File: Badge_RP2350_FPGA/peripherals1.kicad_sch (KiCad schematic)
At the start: 19 parts

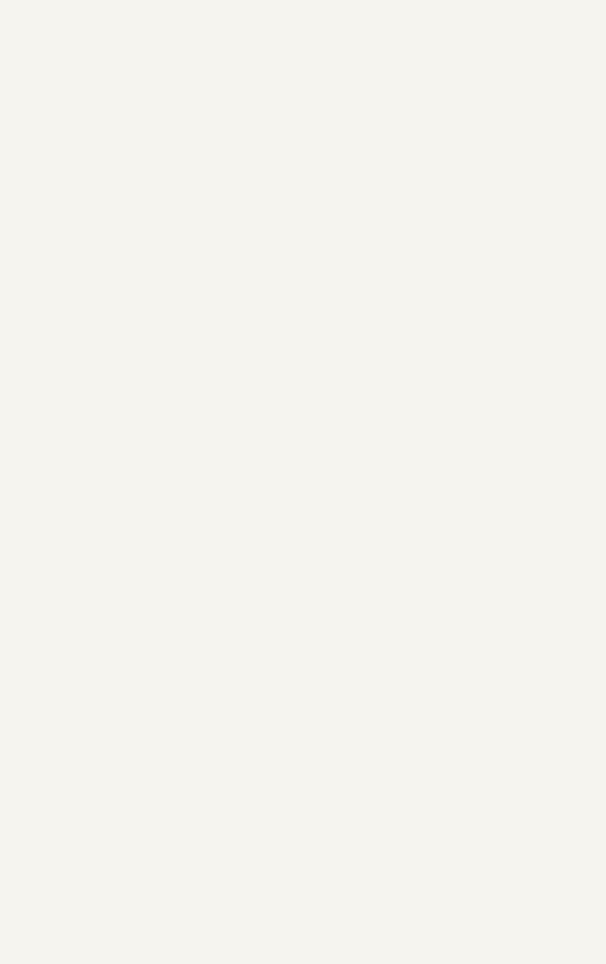
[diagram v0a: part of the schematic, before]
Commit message: add headers and fix voltage references
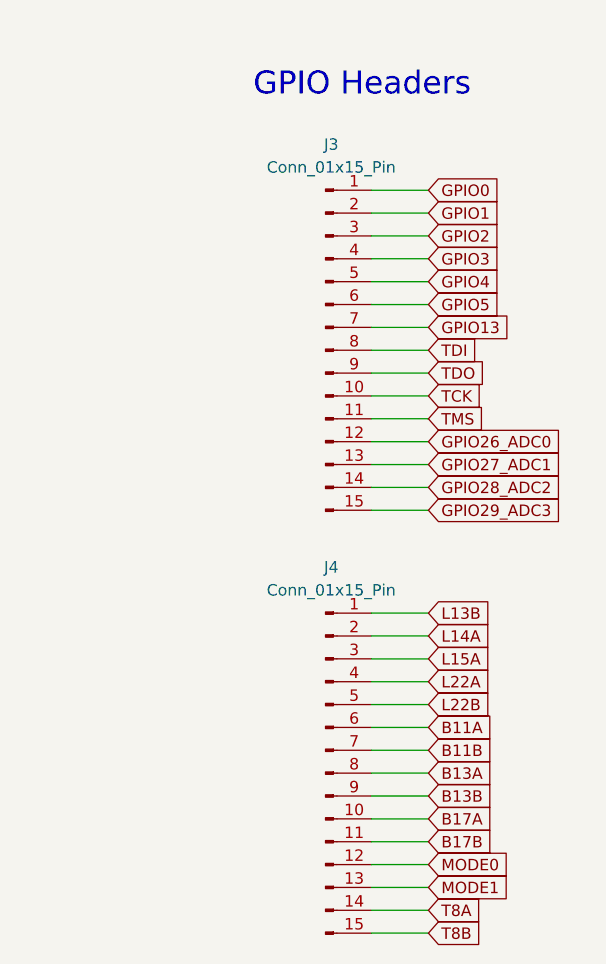
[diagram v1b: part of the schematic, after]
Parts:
- added J3, J4: Conn_01x15_Pin, Connector_PinHeader_2.54mm:PinHeader_1x15_P2.54mm_Vertical, symbol Connector:Conn_01x15_Pin
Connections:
- new net B11A: J4.6 (Pin_6)
- new net B11B: J4.7 (Pin_7)
- new net B13A: J4.8 (Pin_8)
- new net B13B: J4.9 (Pin_9)
- new net B17A: J4.10 (Pin_10)
- new net B17B: J4.11 (Pin_11)
- new net GPIO0: J3.1 (Pin_1)
- new net GPIO1: J3.2 (Pin_2)
- new net GPIO13: J3.7 (Pin_7)
- new net GPIO2: J3.3 (Pin_3)
- new net GPIO26_ADC0: J3.12 (Pin_12)
- new net GPIO27_ADC1: J3.13 (Pin_13)
- new net GPIO28_ADC2: J3.14 (Pin_14)
- new net GPIO29_ADC3: J3.15 (Pin_15)
- new net GPIO3: J3.4 (Pin_4)
- new net GPIO4: J3.5 (Pin_5)
- new net GPIO5: J3.6 (Pin_6)
- new net L13B: J4.1 (Pin_1)
- new net L14A: J4.2 (Pin_2)
- new net L15A: J4.3 (Pin_3)
- new net L22A: J4.4 (Pin_4)
- new net L22B: J4.5 (Pin_5)
- new net MODE0: J4.12 (Pin_12)
- new net MODE1: J4.13 (Pin_13)
- new net T8A: J4.14 (Pin_14)
- new net T8B: J4.15 (Pin_15)
- new net TCK: J3.10 (Pin_10)
- new net TDI: J3.8 (Pin_8)
- new net TDO: J3.9 (Pin_9)
- new net TMS: J3.11 (Pin_11)
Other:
- note added: "GPIO Headers"

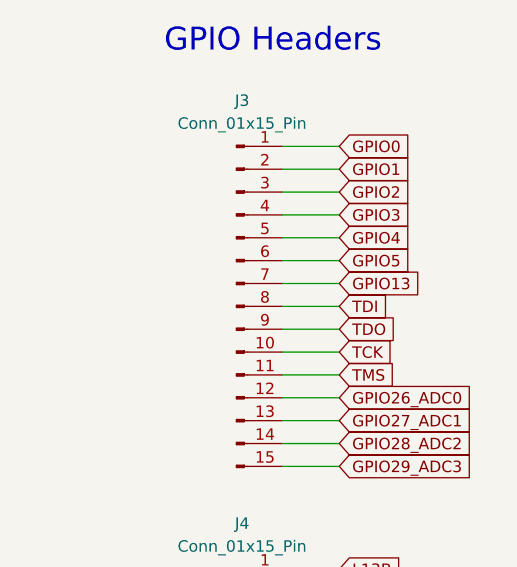
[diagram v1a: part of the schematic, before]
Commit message: add jtagsel_n connection
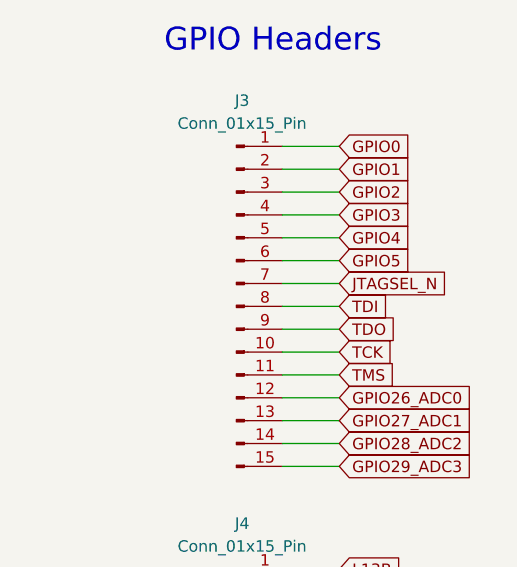
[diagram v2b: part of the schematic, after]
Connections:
- net GPIO13 renamed JTAGSEL_N
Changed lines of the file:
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@@
 		(title "RISC-V Summit Europe Badge")
 		(date "2026-03-29")
-		(rev "v1.4")
+		(rev "v1.42")
 		(company "SemiTO-V, RISC-V Student Team")
 		(comment 3 "License: CERN-OHL-W-2.0")
@@
 		)
 	)
-	(global_label "GPIO13"
+	(global_label "T8A"
+		(shape input)
+		(at 177.8 119.38 0)
+		(fields_autoplaced yes)
+		(effects
+			(font
+				(size 1.27 1.27)
+			)
+			(justify left)
+		)
+		(property "Intersheetrefs" "${INTERSHEET_REFS}"
+			(at 184.0509 119.38 0)
+			(hide yes)
+			(show_name no)
+			(do_not_autoplace no)
+			(effects
+				(font
+					(size 1.27 1.27)
+				)
+				(justify left)
+			)
+		)
+	)
+	(global_label "JTAGSEL_N"
 		(shape input)
 		(at 177.8 54.61 0)
@@
 		)
 		(property "Intersheetrefs" "${INTERSHEET_REFS}"
-			(at 187.6795 54.61 0)
-			(hide yes)
-			(show_name no)
-			(do_not_autoplace no)
-			(effects
-				(font
-					(size 1.27 1.27)
-				)
-				(justify left)
-			)
-		)
-	)
-	(global_label "T8A"
-		(shape input)
-		(at 177.8 119.38 0)
-		(fields_autoplaced yes)
-		(effects
-			(font
-				(size 1.27 1.27)
-			)
-			(justify left)
-		)
-		(property "Intersheetrefs" "${INTERSHEET_REFS}"
-			(at 184.0509 119.38 0)
-			(hide yes)
-			(show_name no)
+			(at 190.7637 54.61 0)
+			(hide yes)
+			(show_name no)

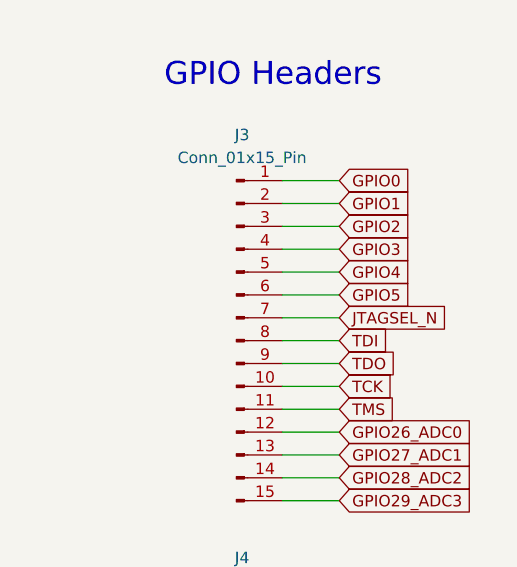
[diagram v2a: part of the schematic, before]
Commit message: add more FPGA connections and generate netlist, bom
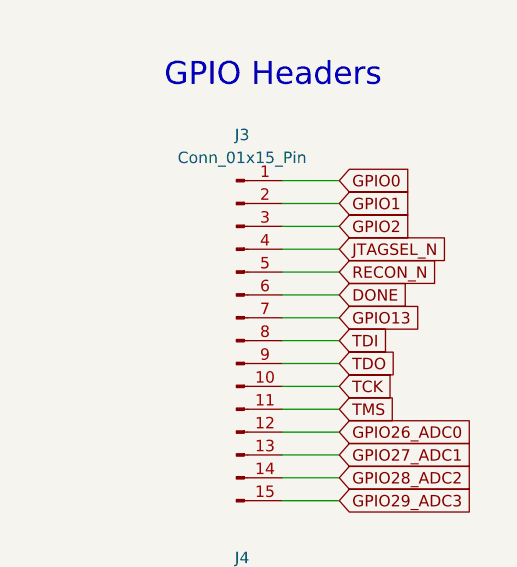
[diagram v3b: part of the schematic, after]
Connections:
- net GPIO3 is gone; now on net JTAGSEL_N: J3.4 (Pin_4)
- net JTAGSEL_N: no longer J3.7 (Pin_7)
- net GPIO4 renamed RECON_N
- net GPIO5 renamed DONE
- new net GPIO13: J3.7 (Pin_7)

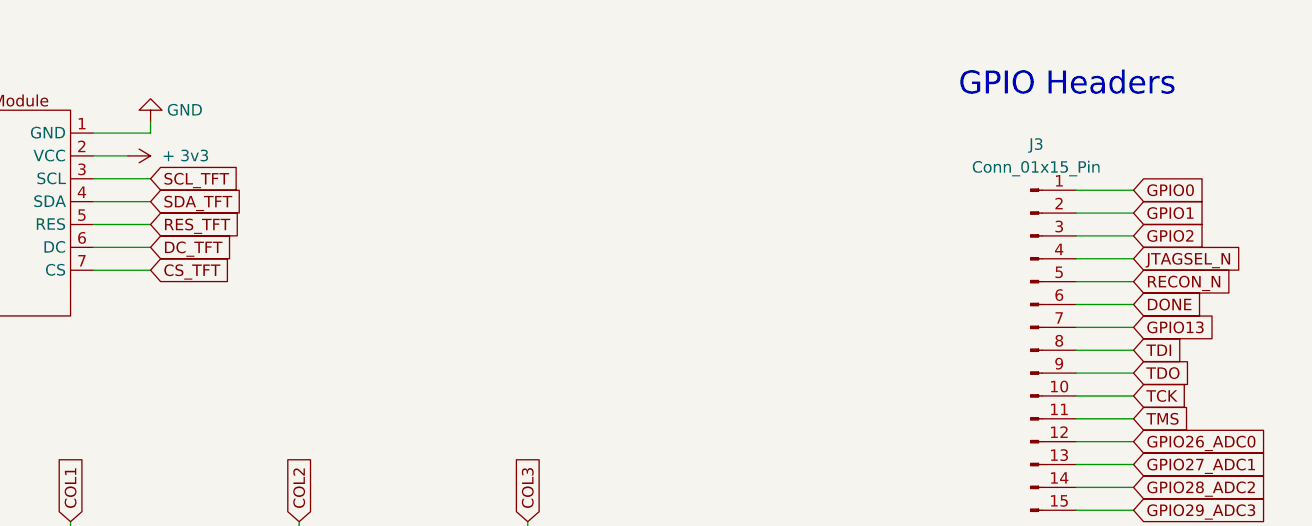
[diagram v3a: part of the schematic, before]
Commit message: update footprints, connections, some labels and more
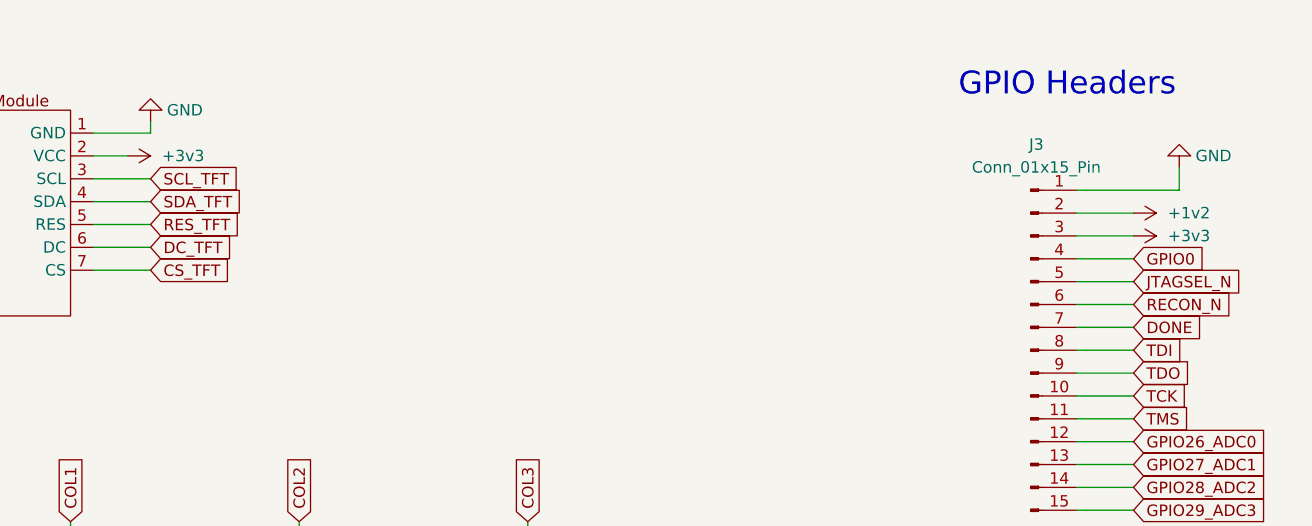
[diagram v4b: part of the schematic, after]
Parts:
- D1, D10, D11, D2, D3, D5, D6, D7, D9: footprint Diode_SMD:D_SOD-123 -> semitovpartslibrary:Nexperia BAS516,115
- SW10, SW11, SW3, SW4, SW5, SW6, SW7, SW8, SW9: footprint Button_Switch_SMD:SW_SPST_PTS647_Sx38 -> semitovpartslibrary:SHOU HAN TS665PA 250gf
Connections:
- net GPIO13 is gone; now on net DONE: J3.7 (Pin_7)
- net GPIO2 is gone; now on net +3v3: J3.3 (Pin_3)
- net DONE: no longer J3.6 (Pin_6)
- net GND: now also J3.1 (Pin_1)
- net GPIO0: now also J3.4 (Pin_4); no longer J3.1 (Pin_1)
- net JTAGSEL_N: now also J3.5 (Pin_5); no longer J3.4 (Pin_4)
- net RECON_N: now also J3.6 (Pin_6); no longer J3.5 (Pin_5)
- net + 3v3 renamed +3v3
- net GPIO1 renamed +1v2
